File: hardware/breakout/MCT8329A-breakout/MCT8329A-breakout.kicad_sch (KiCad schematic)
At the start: 15 parts, among them J1 Conn_01x15, J2 Conn_01x18, U1 MCT8329A

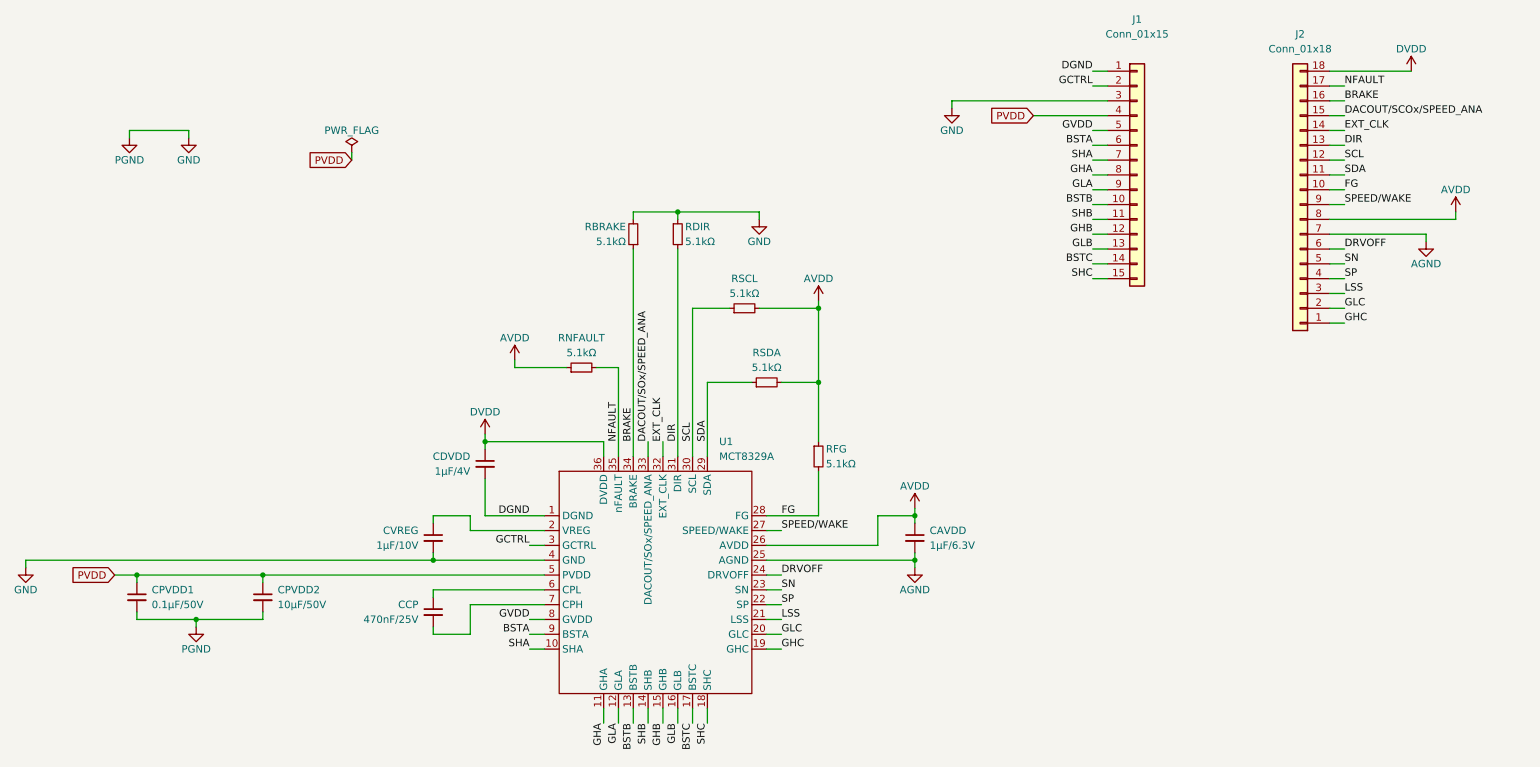
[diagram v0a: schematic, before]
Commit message: Add PCB for MCT8328A breakout.
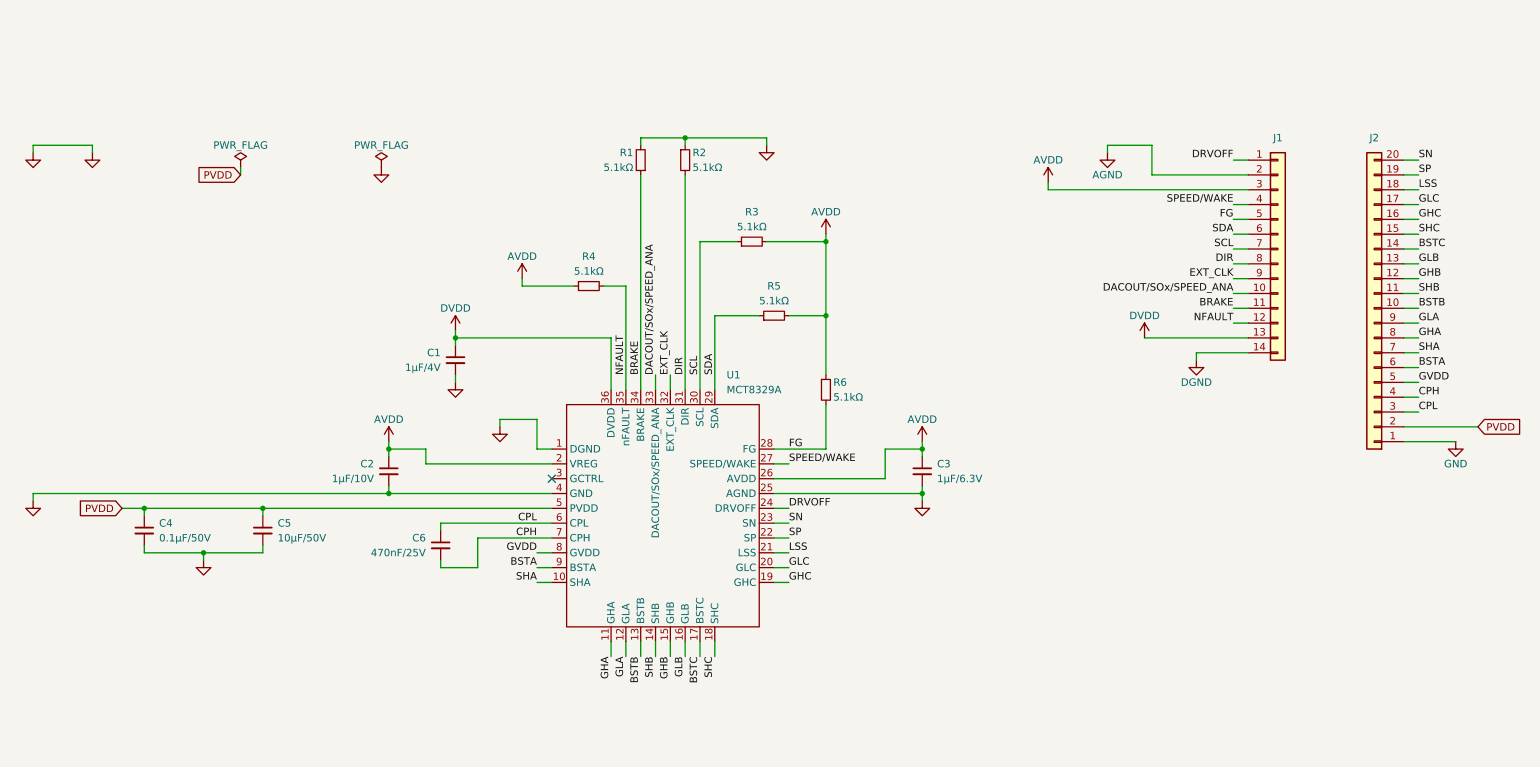
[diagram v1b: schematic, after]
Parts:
- removed CAVDD: 1µF/6.3V, symbol Device:C_Small
- removed J1: Conn_01x15, symbol Connector_Generic:Conn_01x15
- removed J2: Conn_01x18, symbol Connector_Generic:Conn_01x18
- added C3: 1µF/6.3V, Capacitor_SMD:C_0603_1608Metric_Pad1.08x0.95mm_HandSolder, symbol Device:C_Small
- added J1: Conn_01x14, Connector_PinHeader_2.54mm:PinHeader_1x14_P2.54mm_Vertical, symbol Connector_Generic:Conn_01x14
- added J2: Conn_01x20, Connector_PinHeader_2.54mm:PinHeader_1x20_P2.54mm_Vertical, symbol Connector_Generic:Conn_01x20
- C1: renamed from CDVDD; footprint (none) -> Capacitor_SMD:C_0603_1608Metric_Pad1.08x0.95mm_HandSolder
- C2: renamed from CVREG; footprint (none) -> Capacitor_SMD:C_0603_1608Metric_Pad1.08x0.95mm_HandSolder
- C4: renamed from CPVDD1; footprint (none) -> Capacitor_SMD:C_0603_1608Metric_Pad1.08x0.95mm_HandSolder
- C5: renamed from CPVDD2; footprint (none) -> Capacitor_SMD:C_0805_2012Metric_Pad1.18x1.45mm_HandSolder
- C6: renamed from CCP; footprint (none) -> Capacitor_SMD:C_0603_1608Metric_Pad1.08x0.95mm_HandSolder
- R1: renamed from RBRAKE; footprint (none) -> Resistor_SMD:R_0603_1608Metric_Pad0.98x0.95mm_HandSolder
- R2: renamed from RDIR; footprint (none) -> Resistor_SMD:R_0603_1608Metric_Pad0.98x0.95mm_HandSolder
- R3: renamed from RSCL; footprint (none) -> Resistor_SMD:R_0603_1608Metric_Pad0.98x0.95mm_HandSolder
- R4: renamed from RNFAULT; footprint (none) -> Resistor_SMD:R_0603_1608Metric_Pad0.98x0.95mm_HandSolder
- R5: renamed from RSDA; footprint (none) -> Resistor_SMD:R_0603_1608Metric_Pad0.98x0.95mm_HandSolder
- R6: renamed from RFG; footprint (none) -> Resistor_SMD:R_0603_1608Metric_Pad0.98x0.95mm_HandSolder
- U1: footprint (none) -> Texas_Instruments:MCT8329A1IREER
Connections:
- net AGND: now also C3.2, J1.2 (Pin_2)
- net AVDD: now also C2.1, U1.2 (VREG), C3.1, J1.3 (Pin_3)
- net BRAKE: now also J1.11 (Pin_11)
- net BSTA: now also J2.6 (Pin_6)
- net BSTB: now also J2.10 (Pin_10)
- net BSTC: now also J2.14 (Pin_14)
- net DACOUT/SOx/SPEED_ANA: now also J1.10 (Pin_10)
- net DGND: now also J1.14 (Pin_14); no longer C1.2
- net DIR: now also J1.8 (Pin_8)
- net DRVOFF: now also J1.1 (Pin_1)
- net DVDD: now also J1.13 (Pin_13)
- net EXT_CLK: now also J1.9 (Pin_9)
- net FG: now also J1.5 (Pin_5)
- net GHA: now also J2.8 (Pin_8)
- net GHB: now also J2.12 (Pin_12)
- net GHC: now also J2.16 (Pin_16)
- net GLA: now also J2.9 (Pin_9)
- net GLB: now also J2.13 (Pin_13)
- net GLC: now also J2.17 (Pin_17)
- net GND: now also C1.2, U1.37 (PGND), J2.1 (Pin_1)
- net GVDD: now also J2.5 (Pin_5)
- net LSS: now also J2.18 (Pin_18)
- net NFAULT: now also J1.12 (Pin_12)
- net PVDD: now also J2.2 (Pin_2)
- net SCL: now also J1.7 (Pin_7)
- net SDA: now also J1.6 (Pin_6)
- net SHA: now also J2.7 (Pin_7)
- net SHB: now also J2.11 (Pin_11)
- net SHC: now also J2.15 (Pin_15)
- net SN: now also J2.20 (Pin_20)
- net SP: now also J2.19 (Pin_19)
- net SPEED/WAKE: now also J1.4 (Pin_4)
- net CPL: now reaches C6.1, U1.6 (CPL)
- net CPL: now also J2.3 (Pin_3)
- net CPH: now reaches C6.2, U1.7 (CPH)
- net CPH: now also J2.4 (Pin_4)
- net GCTRL: no longer names the net of U1.3 (GCTRL)
- no-connect marks 0 -> 1
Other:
- company: (none) -> Biscuits24_
- title: MCT8329A Breakout (25V Max) -> MCT8329A Breakout (25V max)
- moved on the sheet: C1, C2, C4, C5, C6, R1, R2, R3, R4, R5, R6, U1

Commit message: Finish ooard setup and add pin labels.
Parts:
- added NT1: NetTie_2, NetTie:NetTie-2_SMD_Pad2.0mm, symbol Device:NetTie_2
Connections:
- net GND: now also NT1.2; no longer C1.2, C2.2, C4.2, C5.2, J2.1 (Pin_1), U1.37 (PGND), U1.4 (GND)
- net NFAULT renamed nFAULT
- new net PGND: C1.2, C2.2, C4.2, C5.2, J2.1 (Pin_1), NT1.1, U1.4 (PGND)
